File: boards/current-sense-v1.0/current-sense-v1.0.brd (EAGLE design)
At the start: 70.5 x 94.6 mm, 89 parts, among them IC1 ISO7241, IC2 ISO7241, IC3 ISO7242, IC4 ISO7240, J1 4-PIN_2MM-H, J2 MKS-1658, J3 8-PIN_2MM-H, J6 DF22-2, Q1 IRFH7545, Q2 IRFH7545, Q3 IRFH7545, Q4 IRFH7545, Q5 IRFH7545, Q6 IRFH7545, U1 DRV8303DCA, U13 TLV70233DBVR, U2 INA240PWR, U3 INA240PWR, U4 INA240PWR, U6 ADS8028IRTJT, U7 MPM3620GQV-P, U8 VND5E006ASPTR-E, U9 TLV70433

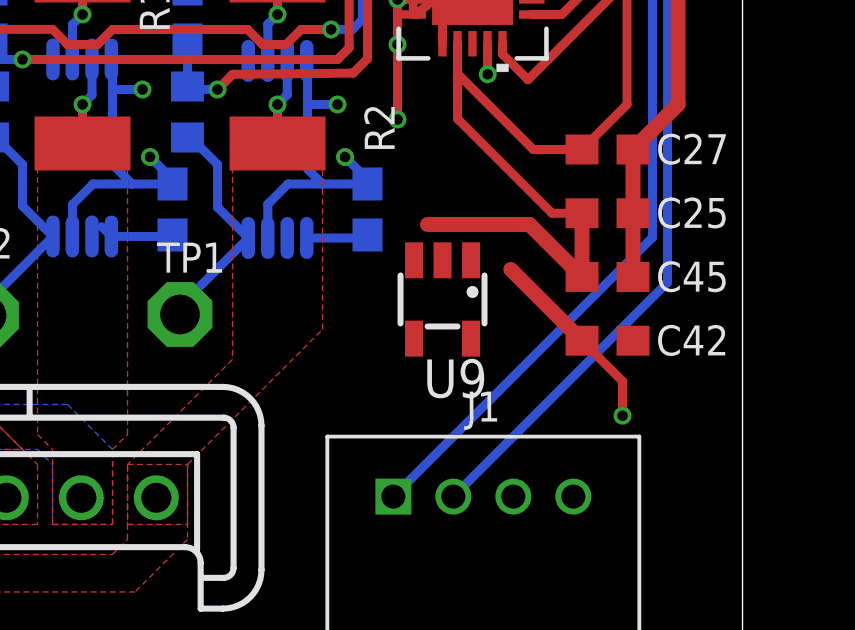
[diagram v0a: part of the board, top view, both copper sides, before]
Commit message: fixed U9 LDO connections
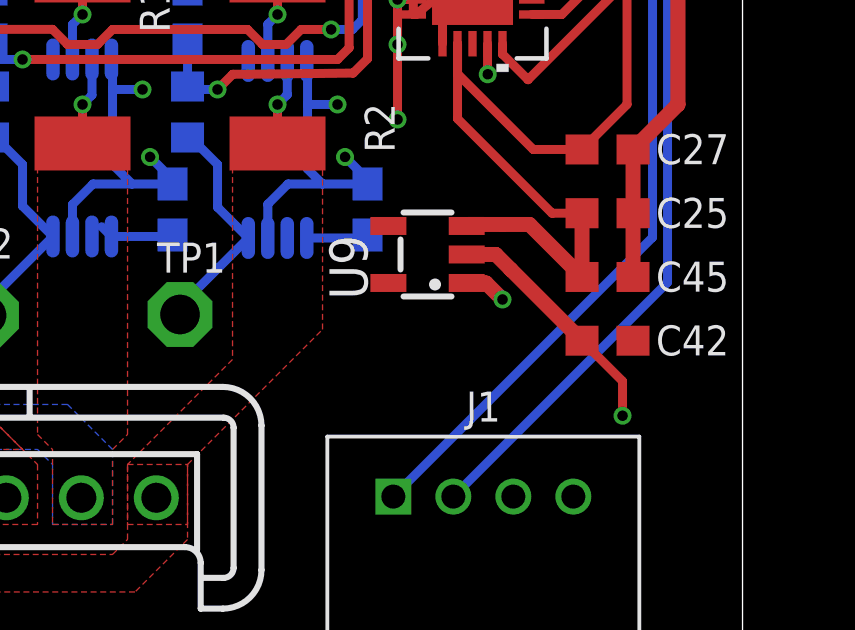
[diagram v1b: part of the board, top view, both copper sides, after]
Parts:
- moved U9 1.58 mm to (60.0, 12.5), turned to 90 degrees
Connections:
- net +18.5V: now also U9.2
- net ADC_3V3: now also U9.3
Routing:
- net +18.5V: track 20.2 -> 21.9 mm
- net GND: track 187.5 -> 188.9 mm, vias 66 -> 67
- net ADC_3V3: track 42.8 -> 41.5 mm
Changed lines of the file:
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@@
 <attribute name="VALUE" x="2.885" y="66.405" size="1.27" layer="27" rot="R180"/>
 </element>
-<element name="U9" library="RoboJackets-PowerICs" package="SOT-23-5" value="TLV70433" x="60.5" y="11" smashed="yes" rot="R180">
-<attribute name="NAME" x="62" y="9" size="1.27" layer="25" ratio="10" rot="R180"/>
+<element name="U9" library="RoboJackets-PowerICs" package="SOT-23-5" value="TLV70433" x="60" y="12.5" smashed="yes" rot="R90">
+<attribute name="NAME" x="58" y="11" size="1.27" layer="25" ratio="10" rot="R90"/>
 </element>
 </elements>
@@
 <contactref element="C42" pad="2"/>
 <contactref element="U9" pad="1"/>
+<wire x1="61.306" y1="11.55" x2="61.95" y2="11.55" width="0.5" layer="1"/>
+<wire x1="61.95" y1="11.55" x2="62.5" y2="11" width="0.5" layer="1"/>
+<via x="62.5" y="11" extent="1-16" drill="0.35"/>
 <wire x1="44.305" y1="58.9" x2="51.925" y2="58.9" width="0" layer="19" extent="1-1"/>
 <wire x1="43" y1="54.75" x2="44.25" y2="57.25" width="0" layer="19" extent="1-1"/>
@@
 <wire x1="62.5" y1="22" x2="61.456621875" y2="22.043378125" width="0" layer="19" extent="1-1"/>
 <wire x1="62.000125" y1="19.525" x2="60.499746875" y2="19.525" width="0" layer="19" extent="1-1"/>
-<wire x1="61.45" y1="12.306" x2="59" y2="17" width="0" layer="19" extent="1-1"/>
 <wire x1="39" y1="21.35" x2="42.975003125" y2="18.950003125" width="0" layer="19" extent="16-16"/>
-<wire x1="66.85" y1="16" x2="62.0074125" y2="18.5074125" width="0" layer="19" extent="1-1"/>
+<wire x1="61.306" y1="11.55" x2="58" y2="14.85" width="0" layer="19" extent="1-16"/>
+<wire x1="66.85" y1="11.75" x2="62.5" y2="11" width="0" layer="19" extent="1-1"/>
 <wire x1="66.85" y1="9.625" x2="66.85" y2="11.75" width="0" layer="19" extent="1-1"/>
 <wire x1="62.86" y1="4.43" x2="66.85" y2="9.625" width="0" layer="19" extent="1-1"/>
@@
 </polygon>
 <wire x1="65.15" y1="9.625" x2="62.775" y2="12" width="0.5" layer="1"/>
+<contactref element="U9" pad="2"/>
+<wire x1="62.775" y1="12" x2="62.275" y2="12.5" width="0.5" layer="1"/>
+<wire x1="62.275" y1="12.5" x2="61.306" y2="12.5" width="0.5" layer="1"/>
 <wire x1="54.5" y1="29.8225" x2="63.07" y2="31.1962" width="0" layer="19" extent="16-16"/>
 <wire x1="48" y1="29.8225" x2="54.5" y2="29.8225" width="0" layer="19" extent="16-16"/>
@@
 <wire x1="34.81" y1="26.585" x2="35" y2="32" width="0" layer="19" extent="1-1"/>
 <wire x1="31.41" y1="26.585" x2="34.81" y2="26.585" width="0" layer="19" extent="1-1"/>
-<wire x1="62.775" y1="12" x2="63.07" y2="31.1962" width="0" layer="19" extent="1-1"/>
+<wire x1="61.306" y1="12.5" x2="54.5" y2="29.8225" width="0" layer="19" extent="1-16"/>
 <wire x1="5.75" y1="48.75" x2="31" y2="34" width="0" layer="19" extent="1-1"/>
 <wire x1="6.1" y1="55.5" x2="5.75" y2="48.75" width="0" layer="19" extent="1-1"/>
@@
 <wire x1="62.5" y1="23.5" x2="62.5" y2="23.474928125" width="0.3" layer="1"/>
 <wire x1="62.5" y1="23.474928125" x2="62.500253125" y2="23.475" width="0.3" layer="1"/>
-<wire x1="65.15" y1="11.75" x2="63.95" y2="12.95" width="0.5" layer="1"/>
+<wire x1="65.15" y1="11.75" x2="63.4" y2="13.5" width="0.5" layer="1"/>
 <wire x1="66.65" y1="21.625" x2="66.65" y2="24.35" width="0.3" layer="1"/>
 <wire x1="66.65" y1="24.35" x2="66.5" y2="24.5" width="0.1524" layer="1"/>
@@
 <via x="63" y="24.5" extent="1-16" drill="0.35"/>
 <wire x1="63" y1="24.5" x2="66.5" y2="24.5" width="0.3" layer="16"/>
-<wire x1="63.95" y1="12.95" x2="63.4" y2="13.5" width="0.5" layer="1"/>
-<wire x1="63.4" y1="13.5" x2="60" y2="13.5" width="0.5" layer="1"/>
+<wire x1="63.4" y1="13.5" x2="62.5" y2="13.5" width="0.5" layer="1"/>
+<contactref element="U9" pad="3"/>
+<wire x1="62.5" y1="13.5" x2="61.356" y2="13.5" width="0.5" layer="1"/>
+<wire x1="61.356" y1="13.5" x2="61.306" y2="13.45" width="0.1524" layer="1"/>
 </signal>
 <signal name="OUT_A">

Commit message: Revert "fixed U9 LDO connections"
This reverts commit 927cff76196117dea27b8f474de1fa187c808058.
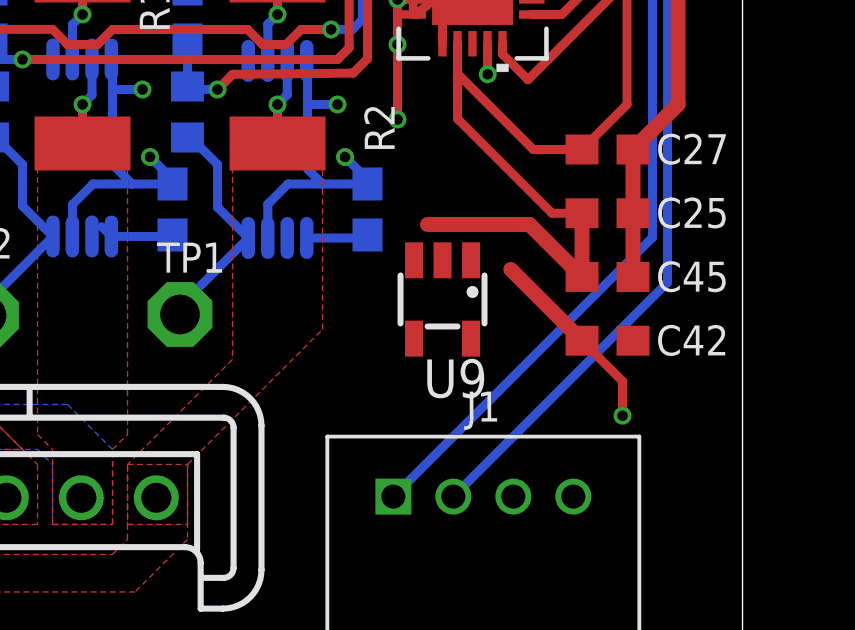
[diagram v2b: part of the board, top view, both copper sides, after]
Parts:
- moved U9 1.58 mm to (60.5, 11.0), turned to 180 degrees
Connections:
- net +18.5V: no longer U9.2
- net ADC_3V3: no longer U9.3
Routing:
- net +18.5V: track 21.9 -> 20.2 mm
- net GND: track 188.9 -> 187.5 mm, vias 67 -> 66
- net ADC_3V3: track 41.5 -> 42.8 mm
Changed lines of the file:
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@@
 <attribute name="VALUE" x="2.885" y="66.405" size="1.27" layer="27" rot="R180"/>
 </element>
-<element name="U9" library="RoboJackets-PowerICs" package="SOT-23-5" value="TLV70433" x="60" y="12.5" smashed="yes" rot="R90">
-<attribute name="NAME" x="58" y="11" size="1.27" layer="25" ratio="10" rot="R90"/>
+<element name="U9" library="RoboJackets-PowerICs" package="SOT-23-5" value="TLV70433" x="60.5" y="11" smashed="yes" rot="R180">
+<attribute name="NAME" x="62" y="9" size="1.27" layer="25" ratio="10" rot="R180"/>
 </element>
 </elements>
@@
 <contactref element="C42" pad="2"/>
 <contactref element="U9" pad="1"/>
-<wire x1="61.306" y1="11.55" x2="61.95" y2="11.55" width="0.5" layer="1"/>
-<wire x1="61.95" y1="11.55" x2="62.5" y2="11" width="0.5" layer="1"/>
-<via x="62.5" y="11" extent="1-16" drill="0.35"/>
 <wire x1="44.305" y1="58.9" x2="51.925" y2="58.9" width="0" layer="19" extent="1-1"/>
 <wire x1="43" y1="54.75" x2="44.25" y2="57.25" width="0" layer="19" extent="1-1"/>
@@
 <wire x1="62.5" y1="22" x2="61.456621875" y2="22.043378125" width="0" layer="19" extent="1-1"/>
 <wire x1="62.000125" y1="19.525" x2="60.499746875" y2="19.525" width="0" layer="19" extent="1-1"/>
+<wire x1="61.45" y1="12.306" x2="59" y2="17" width="0" layer="19" extent="1-1"/>
 <wire x1="39" y1="21.35" x2="42.975003125" y2="18.950003125" width="0" layer="19" extent="16-16"/>
-<wire x1="61.306" y1="11.55" x2="58" y2="14.85" width="0" layer="19" extent="1-16"/>
-<wire x1="66.85" y1="11.75" x2="62.5" y2="11" width="0" layer="19" extent="1-1"/>
+<wire x1="66.85" y1="16" x2="62.0074125" y2="18.5074125" width="0" layer="19" extent="1-1"/>
 <wire x1="66.85" y1="9.625" x2="66.85" y2="11.75" width="0" layer="19" extent="1-1"/>
 <wire x1="62.86" y1="4.43" x2="66.85" y2="9.625" width="0" layer="19" extent="1-1"/>
@@
 </polygon>
 <wire x1="65.15" y1="9.625" x2="62.775" y2="12" width="0.5" layer="1"/>
-<contactref element="U9" pad="2"/>
-<wire x1="62.775" y1="12" x2="62.275" y2="12.5" width="0.5" layer="1"/>
-<wire x1="62.275" y1="12.5" x2="61.306" y2="12.5" width="0.5" layer="1"/>
 <wire x1="54.5" y1="29.8225" x2="63.07" y2="31.1962" width="0" layer="19" extent="16-16"/>
 <wire x1="48" y1="29.8225" x2="54.5" y2="29.8225" width="0" layer="19" extent="16-16"/>
@@
 <wire x1="34.81" y1="26.585" x2="35" y2="32" width="0" layer="19" extent="1-1"/>
 <wire x1="31.41" y1="26.585" x2="34.81" y2="26.585" width="0" layer="19" extent="1-1"/>
-<wire x1="61.306" y1="12.5" x2="54.5" y2="29.8225" width="0" layer="19" extent="1-16"/>
+<wire x1="62.775" y1="12" x2="63.07" y2="31.1962" width="0" layer="19" extent="1-1"/>
 <wire x1="5.75" y1="48.75" x2="31" y2="34" width="0" layer="19" extent="1-1"/>
 <wire x1="6.1" y1="55.5" x2="5.75" y2="48.75" width="0" layer="19" extent="1-1"/>
@@
 <wire x1="62.5" y1="23.5" x2="62.5" y2="23.474928125" width="0.3" layer="1"/>
 <wire x1="62.5" y1="23.474928125" x2="62.500253125" y2="23.475" width="0.3" layer="1"/>
-<wire x1="65.15" y1="11.75" x2="63.4" y2="13.5" width="0.5" layer="1"/>
+<wire x1="65.15" y1="11.75" x2="63.95" y2="12.95" width="0.5" layer="1"/>
 <wire x1="66.65" y1="21.625" x2="66.65" y2="24.35" width="0.3" layer="1"/>
 <wire x1="66.65" y1="24.35" x2="66.5" y2="24.5" width="0.1524" layer="1"/>
@@
 <via x="63" y="24.5" extent="1-16" drill="0.35"/>
 <wire x1="63" y1="24.5" x2="66.5" y2="24.5" width="0.3" layer="16"/>
-<wire x1="63.4" y1="13.5" x2="62.5" y2="13.5" width="0.5" layer="1"/>
-<contactref element="U9" pad="3"/>
-<wire x1="62.5" y1="13.5" x2="61.356" y2="13.5" width="0.5" layer="1"/>
-<wire x1="61.356" y1="13.5" x2="61.306" y2="13.45" width="0.1524" layer="1"/>
+<wire x1="63.95" y1="12.95" x2="63.4" y2="13.5" width="0.5" layer="1"/>
+<wire x1="63.4" y1="13.5" x2="60" y2="13.5" width="0.5" layer="1"/>
 </signal>
 <signal name="OUT_A">

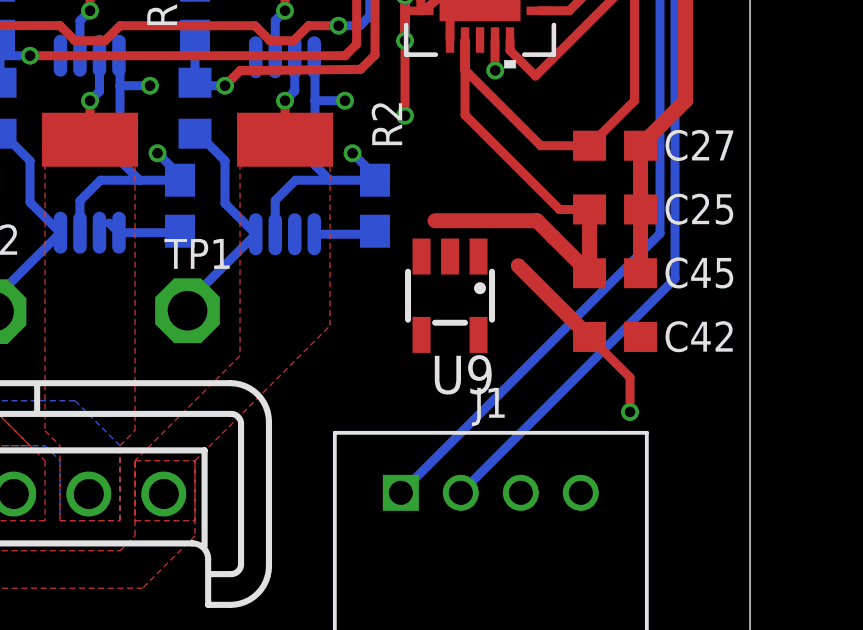
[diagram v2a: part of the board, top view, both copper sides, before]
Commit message: fixed 3V3 connection on LDO
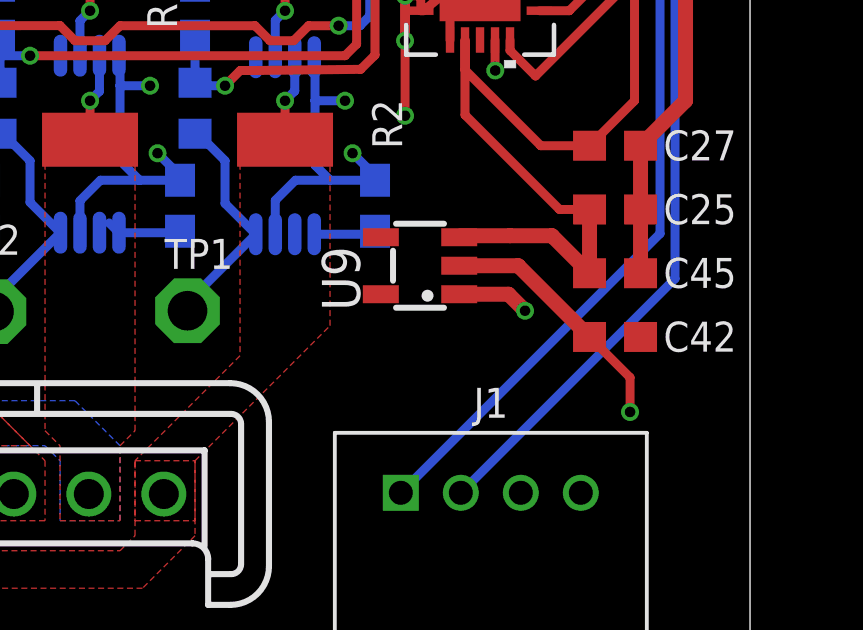
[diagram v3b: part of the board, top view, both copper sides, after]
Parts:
- moved U9 1.41 mm to (59.5, 12.0), turned to 90 degrees
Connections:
- net +18.5V: now also U9.2
- net ADC_3V3: now also U9.3
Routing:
- net GND: track 187.5 -> 189.9 mm, vias 66 -> 67
- net +18.5V: track 20.2 -> 22.2 mm
- net ADC_3V3: track 42.8 -> 41.8 mm
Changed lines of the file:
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@@
 <attribute name="VALUE" x="2.885" y="66.405" size="1.27" layer="27" rot="R180"/>
 </element>
-<element name="U9" library="RoboJackets-PowerICs" package="SOT-23-5" value="TLV70433" x="60.5" y="11" smashed="yes" rot="R180">
-<attribute name="NAME" x="62" y="9" size="1.27" layer="25" ratio="10" rot="R180"/>
+<element name="U9" library="RoboJackets-PowerICs" package="SOT-23-5" value="TLV70433" x="59.5" y="12" smashed="yes" rot="R90">
+<attribute name="NAME" x="57.5" y="10.5" size="1.27" layer="25" ratio="10" rot="R90"/>
 </element>
 </elements>
@@
 <contactref element="C42" pad="2"/>
 <contactref element="U9" pad="1"/>
+<wire x1="60.806" y1="11.05" x2="62.45" y2="11.05" width="0.5" layer="1"/>
+<wire x1="62.45" y1="11.05" x2="63" y2="10.5" width="0.5" layer="1"/>
+<via x="63" y="10.5" extent="1-16" drill="0.35"/>
 <wire x1="44.305" y1="58.9" x2="51.925" y2="58.9" width="0" layer="19" extent="1-1"/>
 <wire x1="43" y1="54.75" x2="44.25" y2="57.25" width="0" layer="19" extent="1-1"/>
@@
 <wire x1="62.5" y1="22" x2="61.456621875" y2="22.043378125" width="0" layer="19" extent="1-1"/>
 <wire x1="62.000125" y1="19.525" x2="60.499746875" y2="19.525" width="0" layer="19" extent="1-1"/>
-<wire x1="61.45" y1="12.306" x2="59" y2="17" width="0" layer="19" extent="1-1"/>
 <wire x1="39" y1="21.35" x2="42.975003125" y2="18.950003125" width="0" layer="19" extent="16-16"/>
-<wire x1="66.85" y1="16" x2="62.0074125" y2="18.5074125" width="0" layer="19" extent="1-1"/>
-<wire x1="66.85" y1="9.625" x2="66.85" y2="11.75" width="0" layer="19" extent="1-1"/>
-<wire x1="62.86" y1="4.43" x2="66.85" y2="9.625" width="0" layer="19" extent="1-1"/>
+<wire x1="60.806" y1="11.05" x2="58" y2="14.85" width="0" layer="19" extent="1-16"/>
+<wire x1="66.85" y1="9.625" x2="63" y2="10.5" width="0" layer="19" extent="1-1"/>
+<wire x1="66.85" y1="11.75" x2="66.85" y2="9.625" width="0" layer="19" extent="1-1"/>
+<wire x1="62.86" y1="4.43" x2="63" y2="10.5" width="0" layer="19" extent="1-1"/>
 <wire x1="35.96" y1="4.39" x2="41.675003125" y2="13.05" width="0" layer="19" extent="16-16"/>
 <wire x1="19.05" y1="15.79" x2="19.35" y2="32.875" width="0" layer="19" extent="16-16"/>
@@
 <vertex x="70.5" y="62.5"/>
 </polygon>
-<wire x1="65.15" y1="9.625" x2="62.775" y2="12" width="0.5" layer="1"/>
+<wire x1="62.775" y1="12" x2="65.15" y2="9.625" width="0.5" layer="1"/>
+<contactref element="U9" pad="2"/>
+<wire x1="60.806" y1="12" x2="62.775" y2="12" width="0.5" layer="1"/>
 <wire x1="54.5" y1="29.8225" x2="63.07" y2="31.1962" width="0" layer="19" extent="16-16"/>
 <wire x1="48" y1="29.8225" x2="54.5" y2="29.8225" width="0" layer="19" extent="16-16"/>
@@
 <wire x1="34.81" y1="26.585" x2="35" y2="32" width="0" layer="19" extent="1-1"/>
 <wire x1="31.41" y1="26.585" x2="34.81" y2="26.585" width="0" layer="19" extent="1-1"/>
-<wire x1="62.775" y1="12" x2="63.07" y2="31.1962" width="0" layer="19" extent="1-1"/>
+<wire x1="60.806" y1="12" x2="54.5" y2="29.8225" width="0" layer="19" extent="1-16"/>
 <wire x1="5.75" y1="48.75" x2="31" y2="34" width="0" layer="19" extent="1-1"/>
 <wire x1="6.1" y1="55.5" x2="5.75" y2="48.75" width="0" layer="19" extent="1-1"/>
@@
 <wire x1="62.5" y1="23.5" x2="62.5" y2="23.474928125" width="0.3" layer="1"/>
 <wire x1="62.5" y1="23.474928125" x2="62.500253125" y2="23.475" width="0.3" layer="1"/>
-<wire x1="65.15" y1="11.75" x2="63.95" y2="12.95" width="0.5" layer="1"/>
+<wire x1="65.15" y1="11.75" x2="63.9" y2="13" width="0.5" layer="1"/>
 <wire x1="66.65" y1="21.625" x2="66.65" y2="24.35" width="0.3" layer="1"/>
 <wire x1="66.65" y1="24.35" x2="66.5" y2="24.5" width="0.1524" layer="1"/>
@@
 <via x="63" y="24.5" extent="1-16" drill="0.35"/>
 <wire x1="63" y1="24.5" x2="66.5" y2="24.5" width="0.3" layer="16"/>
-<wire x1="63.95" y1="12.95" x2="63.4" y2="13.5" width="0.5" layer="1"/>
-<wire x1="63.4" y1="13.5" x2="60" y2="13.5" width="0.5" layer="1"/>
+<wire x1="62.5" y1="13" x2="63.9" y2="13" width="0.5" layer="1"/>
+<contactref element="U9" pad="3"/>
+<wire x1="60.806" y1="12.95" x2="60.856" y2="13" width="0.1524" layer="1"/>
+<wire x1="60.856" y1="13" x2="62.5" y2="13" width="0.5" layer="1"/>
 </signal>
 <signal name="OUT_A">
